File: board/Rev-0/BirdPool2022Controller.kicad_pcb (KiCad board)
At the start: 2 copper layers, 69.8 x 50.8 mm, 27 parts, among them J1 PIC ISP, J2 OSTVN02A150, J3 OSTVN04A150, J4 OSTVN02A150, J5 OSTVN04A150, J6 Conn_01x06, K1 G5LE-14_DC5, U1 PC817, U2 PIC18F1330

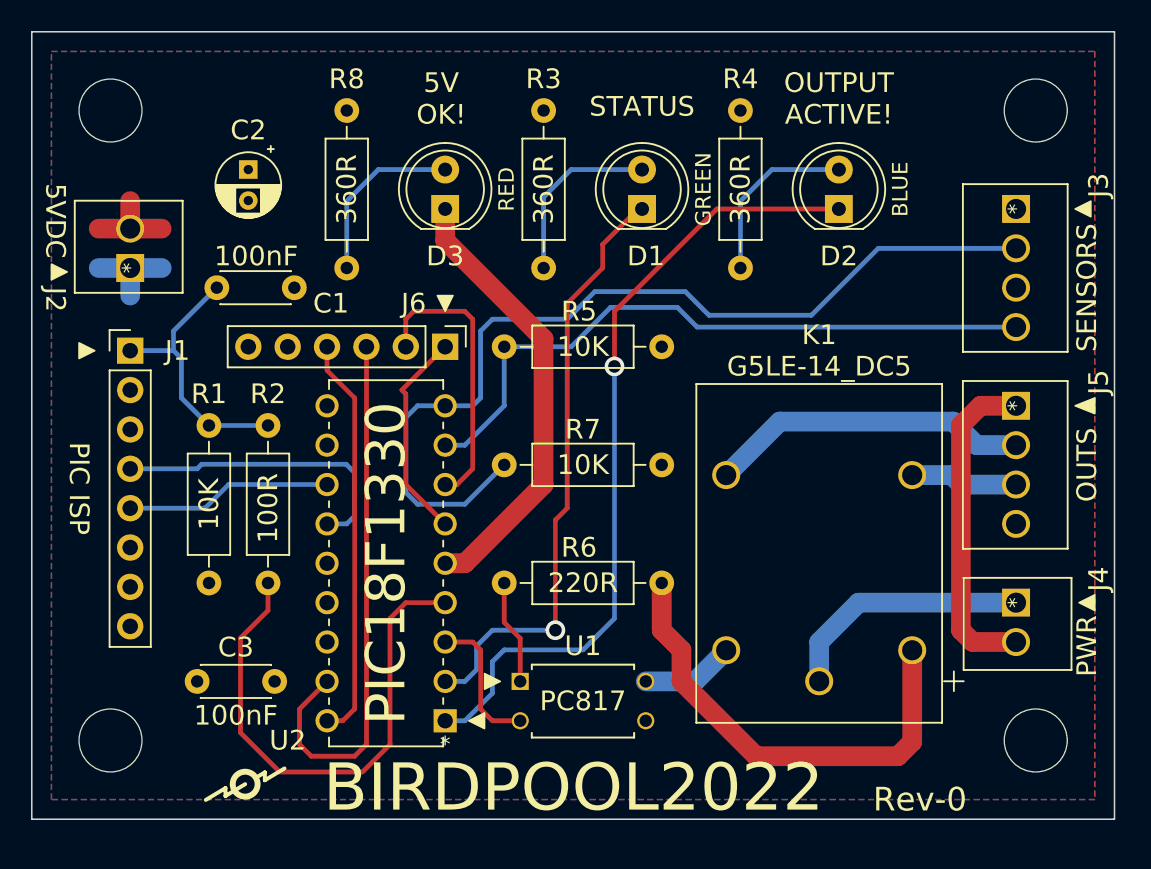
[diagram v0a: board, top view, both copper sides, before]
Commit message: Correction around the relay
ADD: In code, add control of RA4 for the relay for the valve.
ADD: In PCB, add fly wheel diode.
CHG: Rearrange the relay area since the fly wheel diode addition.
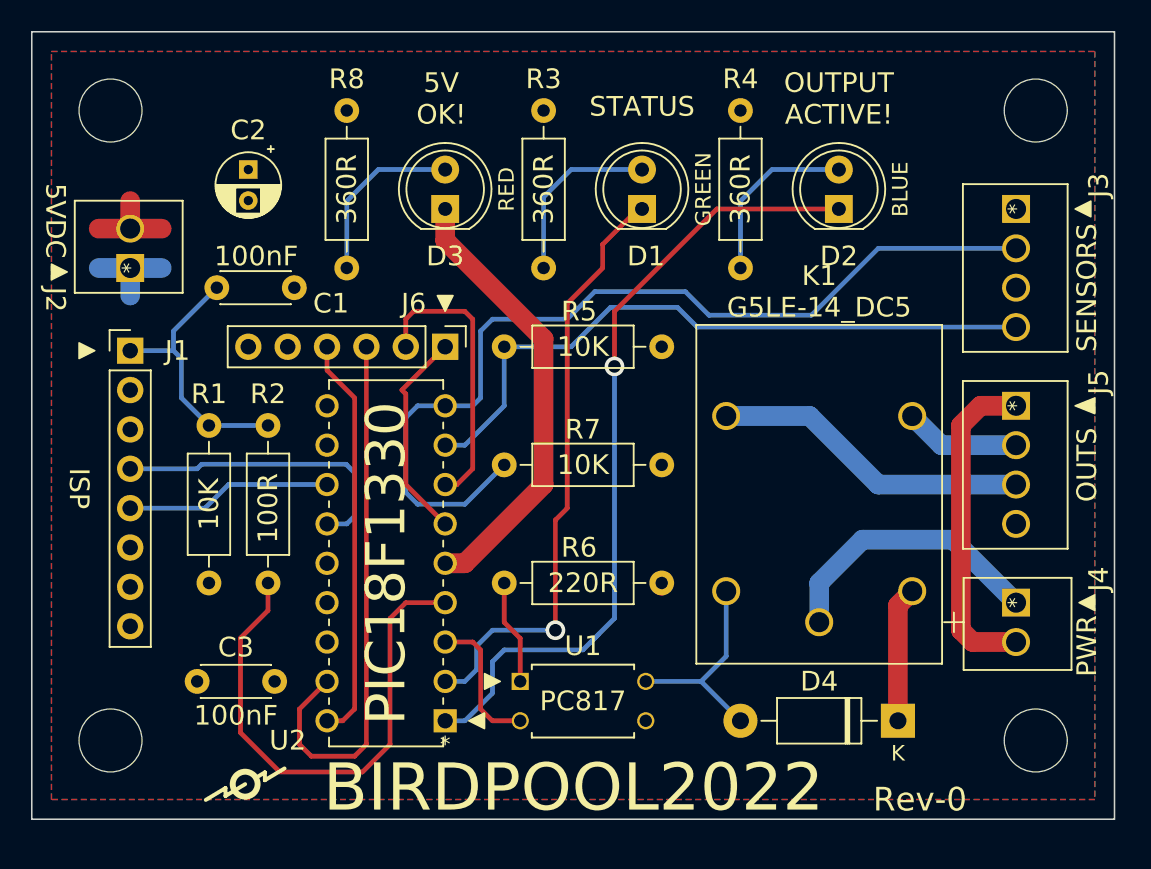
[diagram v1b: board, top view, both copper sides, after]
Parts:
- added D4: 4001, Diode_THT:D_DO-41_SOD81_P10.16mm_Horizontal, F.Cu at (137.2, 100.3)
- J1: value PIC ISP -> ISP
- moved K1 3.81 mm to (132.1, 77.5)
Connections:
- K1 pad 3: Net-(J5-Pad3) -> Net-(J5-Pad2)
- K1 pad 4: Net-(J5-Pad2) -> Net-(J5-Pad3)
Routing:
- net +5V: track 36.1 -> 14.8 mm
- net Net-(J5-Pad3): track 6.95 -> 20.5 mm
- net Net-(J5-Pad2): track 20.8 -> 7.48 mm
- net Net-(D4-Pad2): track 6.02 -> 13.7 mm
- net Net-(J4-Pad1): track 16.3 -> 18.1 mm
